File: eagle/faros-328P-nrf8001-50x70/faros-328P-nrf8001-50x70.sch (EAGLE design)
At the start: 13 parts, among them IC1 ATMEGA328P-PU

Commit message: Added PDF of schematic.
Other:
- note added: "Faros v1.0"
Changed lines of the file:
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@@
 <sheet>
 <plain>
+<text x="121.92" y="-12.7" size="1.778" layer="91">Faros v1.0</text>
 </plain>
 <instances>

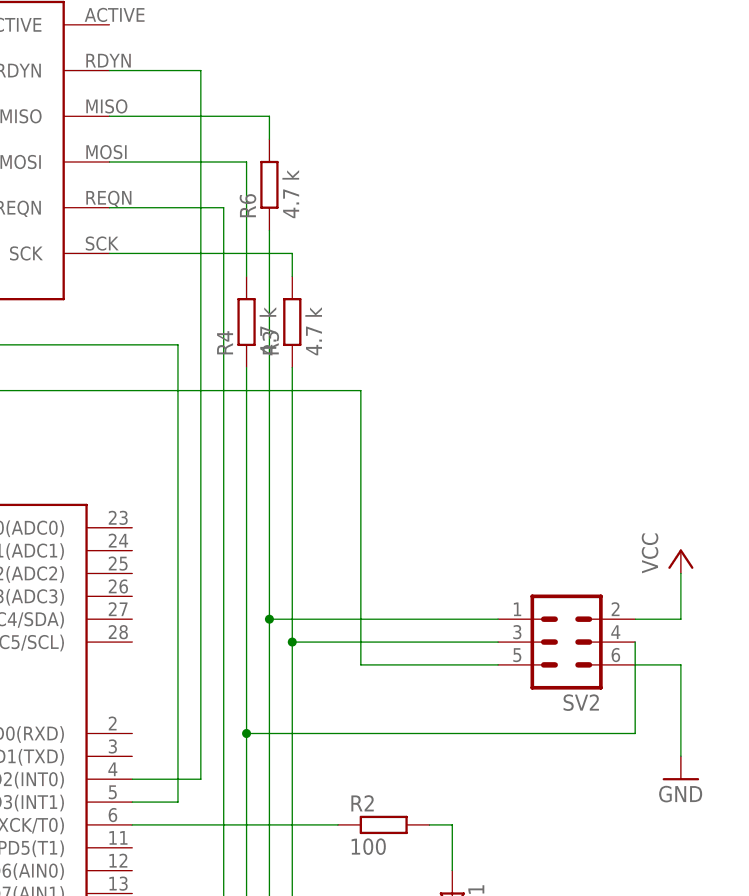
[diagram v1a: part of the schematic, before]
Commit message: Cleaned up part names. Added BOM to readme. Added PDF showing part placement for single-sided board. Updated Gerber files and PCB layout (PDF).
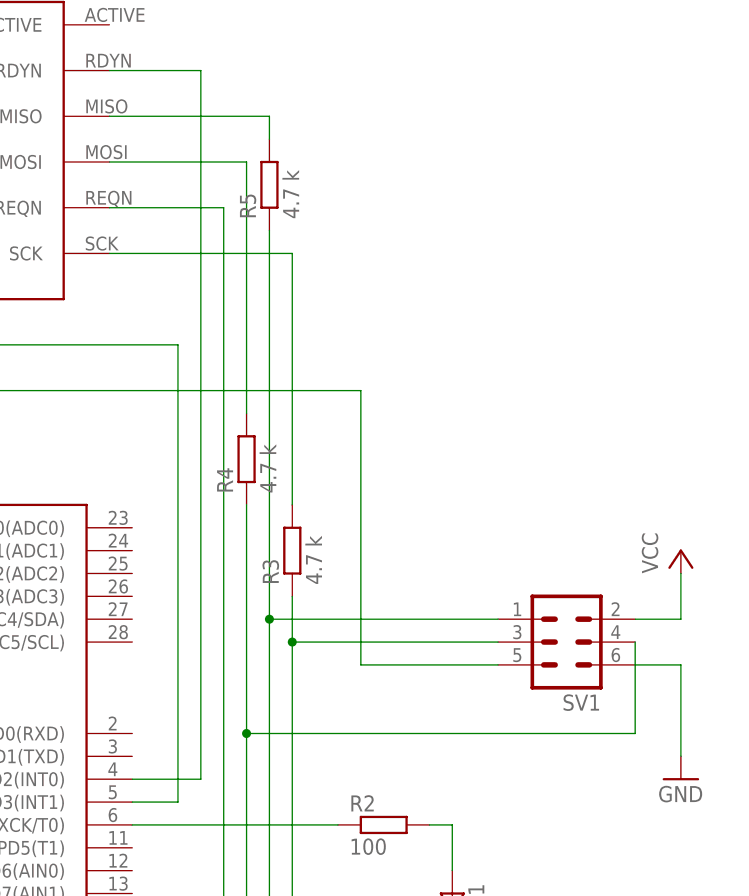
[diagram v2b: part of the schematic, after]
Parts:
- renumbered R6 to R5, SV2 to SV1
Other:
- moved on the sheet: R3, R4
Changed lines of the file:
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@@
 <part name="R2" library="rcl" deviceset="R-EU_" device="0207/7" value="100"/>
 <part name="GND8" library="supply1" deviceset="GND" device=""/>
-<part name="SV2" library="con-lstb" deviceset="MA03-2" device=""/>
+<part name="SV1" library="con-lstb" deviceset="MA03-2" device=""/>
 <part name="R3" library="rcl" deviceset="R-EU_" device="0207/7" value="4.7 k"/>
 <part name="R4" library="rcl" deviceset="R-EU_" device="0207/7" value="4.7 k"/>
-<part name="R6" library="rcl" deviceset="R-EU_" device="0207/7" value="4.7 k"/>
+<part name="R5" library="rcl" deviceset="R-EU_" device="0207/7" value="4.7 k"/>
 </parts>
 <sheets>
@@
 <instance part="R2" gate="G$1" x="99.06" y="12.7"/>
 <instance part="GND8" gate="1" x="106.68" y="-5.08"/>
-<instance part="SV2" gate="1" x="119.38" y="33.02" rot="R180"/>
-<instance part="R3" gate="G$1" x="88.9" y="68.58" rot="R90"/>
-<instance part="R4" gate="G$1" x="83.82" y="68.58" rot="R90"/>
-<instance part="R6" gate="G$1" x="86.36" y="83.82" rot="R90"/>
+<instance part="SV1" gate="1" x="119.38" y="33.02" rot="R180"/>
+<instance part="R3" gate="G$1" x="88.9" y="43.18" rot="R90"/>
+<instance part="R4" gate="G$1" x="83.82" y="53.34" rot="R90"/>
+<instance part="R5" gate="G$1" x="86.36" y="83.82" rot="R90"/>
 </instances>
 <busses>
@@
 <pinref part="P+2" gate="VCC" pin="VCC"/>
 <wire x1="132.08" y1="40.64" x2="132.08" y2="35.56" width="0.1524" layer="91"/>
-<pinref part="SV2" gate="1" pin="2"/>
+<pinref part="SV1" gate="1" pin="2"/>
 <wire x1="132.08" y1="35.56" x2="127" y2="35.56" width="0.1524" layer="91"/>
 </segment>
@@
 </segment>
 <segment>
-<pinref part="SV2" gate="1" pin="6"/>
+<pinref part="SV1" gate="1" pin="6"/>
 <wire x1="127" y1="30.48" x2="132.08" y2="30.48" width="0.1524" layer="91"/>
 <pinref part="GND5" gate="1" pin="GND"/>
@@
 <wire x1="86.36" y1="35.56" x2="86.36" y2="-10.16" width="0.1524" layer="91"/>
 <wire x1="86.36" y1="-10.16" x2="71.12" y2="-10.16" width="0.1524" layer="91"/>
-<pinref part="SV2" gate="1" pin="1"/>
+<pinref part="SV1" gate="1" pin="1"/>
 <wire x1="111.76" y1="35.56" x2="86.36" y2="35.56" width="0.1524" layer="91"/>
-<pinref part="R6" gate="G$1" pin="1"/>
+<pinref part="R5" gate="G$1" pin="1"/>
 <wire x1="86.36" y1="78.74" x2="86.36" y2="35.56" width="0.1524" layer="91"/>
 <junction x="86.36" y="35.56"/>
@@
 <wire x1="2.54" y1="45.72" x2="17.78" y2="45.72" width="0.1524" layer="91"/>
 <junction x="17.78" y="45.72"/>
-<pinref part="SV2" gate="1" pin="5"/>
+<pinref part="SV1" gate="1" pin="5"/>
 <wire x1="111.76" y1="30.48" x2="96.52" y2="30.48" width="0.1524" layer="91"/>
 <wire x1="96.52" y1="30.48" x2="96.52" y2="60.96" width="0.1524" layer="91"/>
@@
 <wire x1="88.9" y1="33.02" x2="88.9" y2="-12.7" width="0.1524" layer="91"/>
 <wire x1="88.9" y1="-12.7" x2="71.12" y2="-12.7" width="0.1524" layer="91"/>
-<pinref part="SV2" gate="1" pin="3"/>
+<pinref part="SV1" gate="1" pin="3"/>
 <wire x1="111.76" y1="33.02" x2="88.9" y2="33.02" width="0.1524" layer="91"/>
 <pinref part="R3" gate="G$1" pin="1"/>
-<wire x1="88.9" y1="63.5" x2="88.9" y2="33.02" width="0.1524" layer="91"/>
+<wire x1="88.9" y1="38.1" x2="88.9" y2="33.02" width="0.1524" layer="91"/>
 <junction x="88.9" y="33.02"/>
 </segment>
@@
 <net name="N$19" class="0">
 <segment>
-<pinref part="SV2" gate="1" pin="4"/>
+<pinref part="SV1" gate="1" pin="4"/>
 <wire x1="127" y1="33.02" x2="127" y2="22.86" width="0.1524" layer="91"/>
 <pinref part="IC1" gate="G$1" pin="PB3(MOSI/OC2)"/>
@@
 <wire x1="127" y1="22.86" x2="83.82" y2="22.86" width="0.1524" layer="91"/>
 <pinref part="R4" gate="G$1" pin="1"/>
-<wire x1="83.82" y1="22.86" x2="83.82" y2="63.5" width="0.1524" layer="91"/>
+<wire x1="83.82" y1="22.86" x2="83.82" y2="48.26" width="0.1524" layer="91"/>
 <junction x="83.82" y="22.86"/>
 </segment>
@@
 <wire x1="68.58" y1="86.36" x2="83.82" y2="86.36" width="0.1524" layer="91"/>
 <pinref part="R4" gate="G$1" pin="2"/>
-<wire x1="83.82" y1="73.66" x2="83.82" y2="86.36" width="0.1524" layer="91"/>
+<wire x1="83.82" y1="58.42" x2="83.82" y2="86.36" width="0.1524" layer="91"/>
 </segment>
 </net>
@@
 <pinref part="MOD1" gate="G$1" pin="MISO"/>
 <wire x1="68.58" y1="91.44" x2="86.36" y2="91.44" width="0.1524" layer="91"/>
-<pinref part="R6" gate="G$1" pin="2"/>
+<pinref part="R5" gate="G$1" pin="2"/>
 <wire x1="86.36" y1="91.44" x2="86.36" y2="88.9" width="0.1524" layer="91"/>
 </segment>
@@
 <wire x1="68.58" y1="76.2" x2="88.9" y2="76.2" width="0.1524" layer="91"/>
 <pinref part="R3" gate="G$1" pin="2"/>
-<wire x1="88.9" y1="76.2" x2="88.9" y2="73.66" width="0.1524" layer="91"/>
-</segment>
-</net>
+<wire x1="88.9" y1="76.2" x2="88.9" y2="48.26" width="0.1524" layer="91"/>
+</segment>
+</net>
